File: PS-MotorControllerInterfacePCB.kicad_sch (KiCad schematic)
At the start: 10 parts, among them U2 MCP16331x-xCH

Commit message: sch
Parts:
- added D4, D8: LED, symbol Device:LED
- added D5, D7: 1N4148WT, Diode_SMD:D_SOD-523, symbol Diode:1N4148WT
- added FID1, FID2, FID3: Fiducial, symbol Mechanical:Fiducial
- added H1, H2, H3, H4: MountingHole, symbol Mechanical:MountingHole
- added J1: 53307-2471, UTSVT_Connectors:PeripheralSOM, symbol utsvt_connectors:PeripheralSOMConnector
- added J2: MotorController-in, symbol Connector_Generic:Conn_02x03_Top_Bottom
- added J3: Conn_01x06, symbol Connector_Generic:Conn_01x06
- added J4: PEAK, symbol Connector_Generic:Conn_01x02
- added J6: MotorController-out, symbol Connector_Generic:Conn_02x03_Top_Bottom
- added LVPWR1, LVPWR2, LVPWR3, LVPWR4, LVPWR5, LVPWR6: LED, LED_SMD:LED_0603_1608Metric, symbol Device:LED
- added R15, R3, R4, R5, R8: 260, symbol Device:R
- added R6, R7, R9: 4.3k, symbol Device:R
- added R_A_TACH_PD1, R_B_TACH_PD1: 10k, symbol Device:R
- added TP1, TP2, TP3, TP4, TP5, TP6: TestPoint, symbol Connector:TestPoint
- added TVS1: PTVS5V0Z1USK, Diode_SMD:Nexperia_DSN1608-2_1.6x0.8mm, symbol Diode:PTVS5V0Z1USK
- C1: value C -> 100n
- C2, C3: value C -> 22u
- D3: value 1N47xxA -> 1N47xxA 7.5V
- L1: value 56m -> 56u
- R1: value R -> 140k
- R2: value R -> 10k
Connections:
- net GND: now also J1.1 (GND), J1.10 (GNDA), J1.3 (GND), J1.5 (GND), J2.2 (Pin_2), J3.2 (Pin_2), LVPWR1.1 (K), LVPWR2.1 (K), LVPWR3.1 (K), LVPWR4.1 (K), LVPWR5.1 (K), LVPWR6.1 (K), TP1.1, TVS1.2 (A)
- net VIN renamed +24V
- net +24V: now also J1.24 (+24V_In), J3.1 (Pin_1), R7.2, TVS1.1 (K)
- net VOUT renamed 12V_BUS
- new net: LVPWR5.2 (A), R8.1
- new net: LVPWR2.2 (A), R3.1
- new net: LVPWR6.2 (A), R15.1
- new net: D4.2 (A), R9.1
- new net: D8.2 (A), R6.1
- new net: LVPWR4.2 (A), R5.1
- new net: LVPWR3.2 (A), R4.1
- new net: LVPWR1.2 (A), R7.1
- new net +12V: J2.1 (Pin_1)
- new net +3V3: J1.2 (+3.3v), R3.2, R_A_TACH_PD1.2, R_B_TACH_PD1.2
- new net CAN_H-in: J2.4 (Pin_4), J3.3 (Pin_3), J4.1 (Pin_1)
- new net CAN_H-out: J1.22 (CAN_H), J6.4 (Pin_4)
- new net CAN_L-in: J2.5 (Pin_5), J3.4 (Pin_4), J4.2 (Pin_2)
- new net CAN_L-out: J1.20 (CAN_L), J6.5 (Pin_5)
- new net FANS_A_NEG: D7.2 (A), D8.1 (K)
- new net FANS_B_NEG: D4.1 (K), D5.2 (A)
- new net FANS_POS: D5.1 (K), D7.1 (K), R6.2, R9.2
- new net FAN_A_TACHO: J1.23 (SPI1_SCK), R5.2, R_A_TACH_PD1.1
- new net FAN_B_TACHO: J1.21 (SPI1_MISO), R8.2, R_B_TACH_PD1.1
- new net PWM_FAN_A: J1.18 (SPI2_SCK), R4.2
- new net PWM_FAN_B: J1.13 (ADC1_IN10), R15.2
- no-connect marks 1 -> 30
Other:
- added sheet Fans (Fans.kicad_sch)
- added sheet Power (Power.kicad_sch)
- note added: "Fiducials"
- note added: "Indicator LEDs"
- note added: "LV PWR indicator LED"
- note added: "Mounting Holes"
- note added: "PSOM"
- note added: "PWR + CAN Connector"
- note added: "Pick TVS with VRWM > LV"
- note added: "Pin: PA11 ; TIM1_CH4"
- note added: "Pin: PA5 ; TIM2_CH1"
- note added: "Pin: PB10 ; TIM2_CH3"
- note added: "Pin: PB3 ; TIM2_CH2"
- note added: "Protection"
- note added: "Testpoints"
- note added: "put close to fan connector and mosfet for small inductive loop"
- note added: "put these near MCU input"
- moved on the sheet: C1, C2, C3, D1, D2, D3, L1, R1, R2, U2

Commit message: schematic
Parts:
- removed C1: 100n, symbol Device:C
- removed C2, C3: 22u, symbol Device:C
- removed D1: D_Schottky, symbol Device:D_Schottky
- removed D2, D5, D7: 1N4148WT, Diode_SMD:D_SOD-523, symbol Diode:1N4148WT
- removed D3: 1N47xxA 7.5V, Diode_THT:D_DO-41_SOD81_P10.16mm_Horizontal, symbol Diode:1N47xxA
- removed D4, D8: LED, symbol Device:LED
- removed FID1, FID2, FID3: Fiducial, symbol Mechanical:Fiducial
- removed H1, H2, H3, H4: MountingHole, symbol Mechanical:MountingHole
- removed L1: 56u, symbol Device:L
- removed LVPWR3, LVPWR4, LVPWR5, LVPWR6: LED, LED_SMD:LED_0603_1608Metric, symbol Device:LED
- removed R1: 140k, symbol Device:R
- removed R15, R4, R5, R8: 260, symbol Device:R
- removed R2: 10k, symbol Device:R
- removed R9: 4.3k, symbol Device:R
- removed U2: MCP16331x-xCH, Package_TO_SOT_SMD:SOT-23-6, symbol Regulator_Switching:MCP16331x-xCH
- added H1, H2, H3, H4: MountingHole_Pad, symbol Mechanical:MountingHole_Pad
- added JP1: TRM, Connector_PinHeader_2.54mm:PinHeader_1x02_P2.54mm_Vertical, symbol Jumper:Jumper_2_Open
- added LVPWR7: LED, LED_SMD:LED_0603_1608Metric, symbol Device:LED
- added R17: 120, Resistor_SMD:R_0603_1608Metric_Pad0.98x0.95mm_HandSolder, symbol Device:R
- R6: value 4.3k -> 1.9k
- TP1: value TestPoint -> TP_GND
- TP2: value TestPoint -> TP_3V3
- TP3: value TestPoint -> TP_A_TACH
- TP4: value TestPoint -> TP_B_TACH
- TP5: value TestPoint -> TP_B_PWM
- TP6: value TestPoint -> TP_A_PWM
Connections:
- net FANS_POS is gone; now on net +12V: R6.2
- net +24V: no longer J3.1 (Pin_1)
- net +3V3: now also TP2.1
- net CAN_H-out: now also J3.5 (Pin_5), R17.1
- net CAN_L-out: now also J3.6 (Pin_6), JP1.2 (B)
- net FAN_A_TACHO: now also TP3.1
- net FAN_B_TACHO: now also TP4.1
- net GND: now also H1.1, H2.1, H3.1, H4.1, LVPWR7.1 (K); no longer J1.10 (GNDA)
- net PWM_FAN_A: now also TP6.1
- net PWM_FAN_B: now also TP5.1
- net at R6.1: now also LVPWR7.2 (A)
- new net: JP1.1 (A), R17.2
- new net VIN_24V: J3.1 (Pin_1)
- no-connect marks 30 -> 23
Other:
- added sheet Buck Converter 24V-12V (BuckConverter.kicad_sch)
- added sheet Fuses (Fuses.kicad_sch)
- note added: "(12-2.5)/(.005) = 1.9k"
- note added: "(24-2.5)/(.005) = 4.3k"
- note added: "(3.3-2.5)/(.005) = 260"
- note added: "CAN Bus Termination"
- note added: "Pick TVS with VRWM > LV (24V)"
- note added: "Route PSOM Last reduce signal reflection"
- note added: "TVS"
- note added: "VCU -> moco-in -> moco-out -> interface terminate on VCU and interface"
- note added: "put PUs near MCU input"
- note removed: "BUCK CONVERTER 24V-12V"
- note removed: "Fiducials"
- note removed: "Pick TVS with VRWM > LV"
- note removed: "Protection"
- note removed: "Testpoints"
- note removed: "put close to fan connector and mosfet for small inductive loop"
- note removed: "put these near MCU input"
- moved on the sheet: J1, J2, J3, J4, J6, LVPWR1, LVPWR2, R3, R7, R_A_TACH_PD1, R_B_TACH_PD1, TVS1

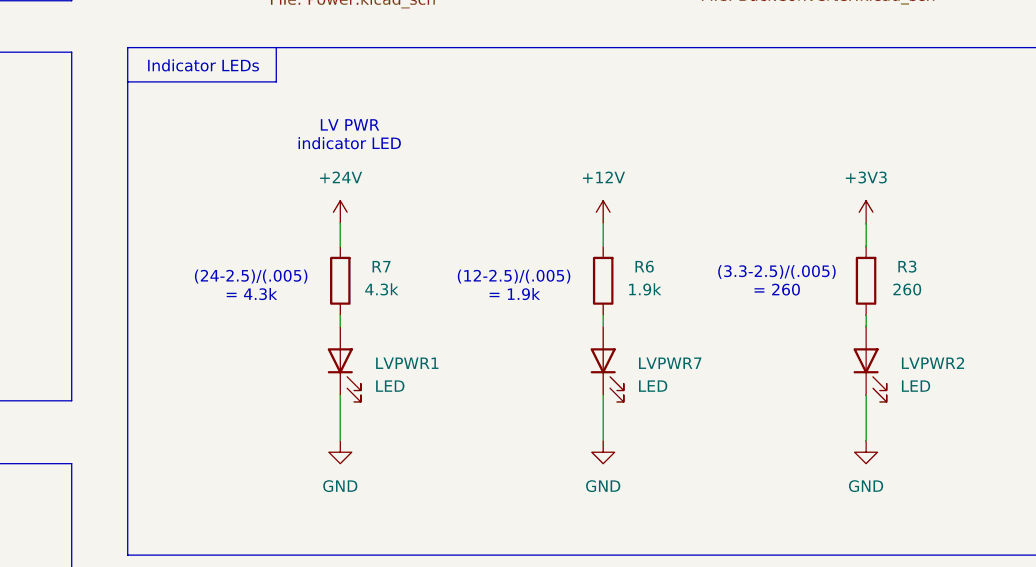
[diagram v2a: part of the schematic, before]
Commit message: added testpoints too
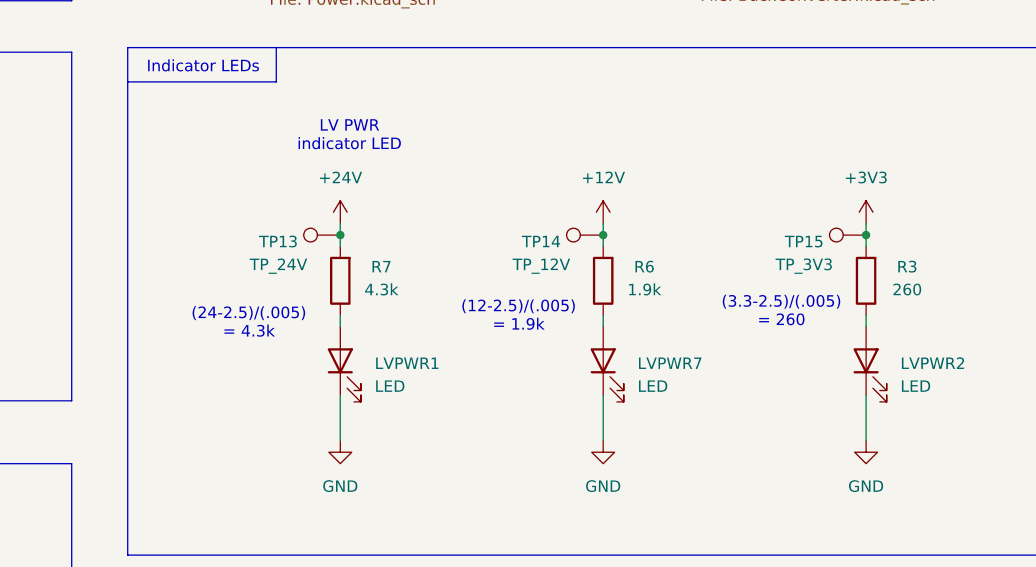
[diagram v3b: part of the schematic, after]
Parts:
- added TP13: TP_24V, symbol Connector:TestPoint
- added TP14: TP_12V, symbol Connector:TestPoint
- added TP15: TP_3V3, symbol Connector:TestPoint
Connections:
- net +12V: now also TP14.1
- net +24V: now also TP13.1
- net +3V3: now also TP15.1
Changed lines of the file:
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@@
 	(text "(24-2.5)/(.005) \n= 4.3k"
 		(exclude_from_sim no)
-		(at 190.754 130.302 0)
+		(at 190.5 134.366 0)
 		(effects
 			(font
@@
 	(text "(12-2.5)/(.005) \n= 1.9k"
 		(exclude_from_sim no)
-		(at 219.964 130.302 0)
+		(at 220.472 133.604 0)
 		(effects
 			(font
@@
 	(text "(3.3-2.5)/(.005) \n= 260"
 		(exclude_from_sim no)
-		(at 249.174 129.794 0)
+		(at 249.682 133.096 0)
 		(effects
 			(font
@@
 	)
 	(junction
+		(at 200.66 124.46)
+		(diameter 0)
+		(color 0 0 0 0)
+	)
+	(junction
 		(at 52.07 78.74)
 		(diameter 0)
@@
 	)
 	(junction
+		(at 259.08 124.46)
+		(diameter 0)
+		(color 0 0 0 0)
+	)
+	(junction
 		(at 133.35 57.15)
 		(diameter 0)
@@
 	)
 	(junction
+		(at 229.87 124.46)
+		(diameter 0)
+		(color 0 0 0 0)
+	)
+	(junction
 		(at 46.99 83.82)
 		(diameter 0)
@@
 	(wire
 		(pts
-			(xy 229.87 123.19) (xy 229.87 125.73)
+			(xy 229.87 123.19) (xy 229.87 124.46)
 		)
 		(stroke
@@
 	(wire
 		(pts
+			(xy 229.87 124.46) (xy 229.87 125.73)
+		)
+		(stroke
+			(width 0)
+			(type default)
+		)
+	)
+	(wire
+		(pts
 			(xy 187.96 81.28) (xy 191.77 81.28)
 		)
@@
 	(wire
 		(pts
-			(xy 200.66 123.19) (xy 200.66 125.73)
+			(xy 200.66 123.19) (xy 200.66 124.46)
 		)
 		(stroke
@@
 	(wire
 		(pts
+			(xy 259.08 124.46) (xy 259.08 125.73)
+		)
+		(stroke
+			(width 0)
+			(type default)
+		)
+	)
+	(wire
+		(pts
 			(xy 133.35 53.34) (xy 133.35 57.15)
 		)
@@
 	(wire
 		(pts
-			(xy 259.08 123.19) (xy 259.08 125.73)
+			(xy 200.66 124.46) (xy 200.66 125.73)
+		)
+		(stroke
+			(width 0)
+			(type default)
+		)
+	)
+	(wire
+		(pts
+			(xy 259.08 123.19) (xy 259.08 124.46)
 		)
 		(stroke
@@
 	)
 	(symbol
+		(lib_id "Connector:TestPoint")
+		(at 200.66 124.46 90)
+		(unit 1)
+		(exclude_from_sim no)
+		(in_bom yes)
+		(on_board yes)
+		(dnp no)
+		(property "Reference" "TP13"
+			(at 193.802 125.222 90)
+			(effects
+				(font
+					(size 1.27 1.27)
+				)
+			)
+		)
+		(property "Value" "TP_24V"
+			(at 193.802 127.762 90)
+			(effects
+				(font
+					(size 1.27 1.27)
+				)
+			)
+		)
+		(property "Footprint" ""
+			(at 200.66 119.38 0)
+			(effects
+				(font
+					(size 1.27 1.27)
+				)
+				(hide yes)
+			)
+		)
+		(property "Datasheet" "~"
+			(at 200.66 119.38 0)
+			(effects
+				(font
+					(size 1.27 1.27)
+				)
+				(hide yes)
+			)
+		)
+		(property "Description" "test point"
+			(at 200.66 124.46 0)
+			(effects
+				(font
+					(size 1.27 1.27)
+				)
+				(hide yes)
+			)
+		)
+		(pin "1"
+		)
+		(instances
+			(project "PS-MotorControllerInterfacePCB"
+				(path "/a2e13c19-ff3a-4e43-a7f5-200fd5b2b978"
+					(reference "TP13")
+					(unit 1)
+				)
+			)
+		)
+	)
+	(symbol
 		(lib_id "Connector_Generic:Conn_02x03_Top_Bottom")
 		(at 48.26 181.61 0)
@@
 	)
 	(symbol
+		(lib_id "Connector:TestPoint")
+		(at 259.08 124.46 90)
+		(unit 1)
+		(exclude_from_sim no)
+		(in_bom yes)
+		(on_board yes)
+		(dnp no)
+		(property "Reference" "TP15"
+			(at 252.222 125.222 90)
+			(effects
+				(font
+					(size 1.27 1.27)
+				)
+			)
+		)
+		(property "Value" "TP_3V3"
+			(at 252.222 127.762 90)
+			(effects
+				(font
+					(size 1.27 1.27)
+				)
+			)
+		)
+		(property "Footprint" ""
+			(at 259.08 119.38 0)
+			(effects
+				(font
+					(size 1.27 1.27)
+				)
+				(hide yes)
+			)
+		)
+		(property "Datasheet" "~"
+			(at 259.08 119.38 0)
+			(effects
+				(font
+					(size 1.27 1.27)
+				)
+				(hide yes)
+			)
+		)
+		(property "Description" "test point"
+			(at 259.08 124.46 0)
+			(effects
+				(font
+					(size 1.27 1.27)
+				)
+				(hide yes)
+			)
+		)
+		(pin "1"
+		)
+		(instances
+			(project "PS-MotorControllerInterfacePCB"
+				(path "/a2e13c19-ff3a-4e43-a7f5-200fd5b2b978"
+					(reference "TP15")
+					(unit 1)
+				)
+			)
+		)
+	)
+	(symbol
 		(lib_id "Device:R")
 		(at 229.87 129.54 180)
@@
 					(unit 1)
 				)
+			)
+		)
+	)
+	(symbol
+		(lib_id "Connector:TestPoint")
+		(at 229.87 124.46 90)
+		(unit 1)
+		(exclude_from_sim no)
+		(in_bom yes)
+		(on_board yes)
+		(dnp no)
+		(property "Reference" "TP14"
+			(at 223.012 125.222 90)
+			(effects
+				(font
+					(size 1.27 1.27)
+				)
+			)
+		)
+		(property "Value" "TP_12V"
+			(at 223.012 127.762 90)
+			(effects
+				(font
+					(size 1.27 1.27)
+				)
+			)
+		)
+		(property "Footprint" ""
+			(at 229.87 119.38 0)
+			(effects
+				(font
+					(size 1.27 1.27)
+				)
+				(hide yes)
+			)
+		)
+		(property "Datasheet" "~"
+			(at 229.87 119.38 0)
+			(effects
+				(font
+					(size 1.27 1.27)
+				)
+				(hide yes)
+			)
+		)
+		(property "Description" "test point"
+			(at 229.87 124.46 0)
+			(effects
+				(font
+					(size 1.27 1.27)
+				)
+				(hide yes)
+			)
+		)
+		(pin "1"
+		)
+		(instances
+			(project "PS-MotorControllerInterfacePCB"
+				(path "/a2e13c19-ff3a-4e43-a7f5-200fd5b2b978"
+					(reference "TP14")
+					(unit 1)
+				)

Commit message: changes + ioc
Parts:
- added LVPWR4, LVPWR5, LVPWR8, LVPWR9: LED, LED_SMD:LED_0603_1608Metric, symbol Device:LED
- added R11: 100k, Resistor_SMD:R_0603_1608Metric, symbol Device:R_US
- added R12: 9。5k, Resistor_SMD:R_0603_1608Metric, symbol Device:R_US
- added R18: 200k, Resistor_SMD:R_0603_1608Metric, symbol Device:R_US
- added R21, R22, R5, R8: 5k, symbol Device:R
- added R25: 9k, Resistor_SMD:R_0603_1608Metric, symbol Device:R_US
- added TP9: TP_3V3, symbol Connector:TestPoint
- added Z1, Z2: SMAF4751A-TP, UTSVT_Passives:SODFL5026X125N, symbol UTSVT_Power:SMAF4749A-TP
- added Z3, Z4: SMAF4744A, UTSVT_Passives:SODFL5026X125N, symbol UTSVT_Power:SMAF4749A-TP
- R3: value 260 -> 5k
- R6: value 1.9k -> 5k
- R7: value 4.3k -> 5k
- TP2: value TP_3V3 -> TP_24V
- TP5: value TP_B_PWM -> TP_12V
- TP6: value TP_A_PWM -> TP_3V3
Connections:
- net +3V3: no longer TP2.1
- net 12V_BUS: now also R11.1, Z4.1 (K)
- net CAN_H-out: no longer J3.5 (Pin_5), J6.4 (Pin_4)
- net CAN_L-out: no longer J3.6 (Pin_6), J6.5 (Pin_5)
- net GND: now also LVPWR4.1 (K), LVPWR5.1 (K), LVPWR8.1 (K), LVPWR9.1 (K), R12.2, R25.2, Z1.2 (A), Z2.2 (A), Z3.2 (A), Z4.2 (A); no longer H1.1, H2.1, H3.1, H4.1
- net PWM_FAN_A: no longer TP6.1
- net PWM_FAN_B: no longer TP5.1
- net VIN_24V: now also R18.1, Z1.1 (K)
- net LED2: now reaches J1.11 (ADC1_IN9)
- net D_C: now reaches J1.12 (SPI2_NSS)
- net D_C: now also TP6.1, R21.2
- net M_FAULT: now reaches J1.14 (SPI2_MISO)
- net M_FAULT: now also R22.2, TP9.1
- net LED3: now reaches J1.15 (ADC1_IN11)
- net LED: now reaches J1.16 (SPI2_MOSI)
- net LED5: now reaches J1.17 (SPI1_MOSI)
- net LED4: now reaches J1.19 (SPI1_NSS)
- net S_OC: now reaches J1.4 (I2C1_SDA)
- net S_OC: now also TP5.1, R8.2
- net MESSAGE: now reaches J1.6 (I2C1_SCL)
- net MESSAGE: now also TP2.1, R5.2
- net LED1: now reaches J1.9 (ADC1_IN7)
- net CAN_H-in renamed CAN_H
- net CAN_H: now also J3.5 (Pin_5), J6.4 (Pin_4)
- net CAN_L-in renamed CAN_L
- net CAN_L: now also J3.6 (Pin_6), J6.5 (Pin_5)
- new net: LVPWR4.2 (A), R5.1
- new net: LVPWR9.2 (A), R22.1
- new net: LVPWR8.2 (A), R21.1
- new net: LVPWR5.2 (A), R8.1
- new net Power12V/OV: R11.2, R12.1
- new net Power24V/OV: R18.2, R25.1
- new net RPP_EN12: Z3.1 (K)
- new net RPP_EN24: Z2.1 (K)
- no-connect marks 23 -> 17
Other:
- sheet Fuses renamed Fuse
- removed sheet Power
- added sheet Power12V (Power.kicad_sch)
- added sheet Power24V (Power.kicad_sch)
- added sheet StatusLEDs (StatusLEDs.kicad_sch)
- note added: "PA12"
- note added: "PA2"
- note added: "PA4"
- note added: "PA6"
- note added: "PB0"
- note added: "PB15"
- note added: "Pin: PB12"
- note added: "Pin: PB14"
- note added: "Pin: PB6"
- note added: "Pin: PB7"
- note removed: "(12-2.5)/(.005) = 1.9k"
- note removed: "(24-2.5)/(.005) = 4.3k"
- note removed: "(3.3-2.5)/(.005) = 260"
- moved on the sheet: H1, H2, H3, H4, JP1, LVPWR1, LVPWR2, LVPWR7, R17, R3, R6, R7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

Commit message: small fix
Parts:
- TP2: value TP_24V -> TP_M
- TP5: value TP_12V -> TP_OC
- TP6: value TP_3V3 -> TP_D_C
- TP9: value TP_3V3 -> TP_F
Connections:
- net CAN_H-out is gone; now on net CAN_H: J1.22 (CAN_H), R17.1
- net CAN_L-out is gone; now on net CAN_L: J1.20 (CAN_L), JP1.2 (B)
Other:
- note added: "PB14"
- note added: "PB6"
- note added: "PB7"
- note removed: "Pin: PB14"
- note removed: "Pin: PB6"
- note removed: "Pin: PB7"
- moved on the sheet: J1, J2, J3, J4, J6, JP1, LVPWR1, LVPWR2, LVPWR4, LVPWR5, LVPWR7, LVPWR8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

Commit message: layout
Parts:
- removed TP13: TP_24V, symbol Connector:TestPoint
- removed TP14: TP_12V, symbol Connector:TestPoint
- added J5: Power MPPT, UTSVT_Connectors:Molex_Nano-Fit_105309-xx02_1x02_P2.50mm_Vertical, symbol Connector_Generic:Conn_01x02
- H1, H2, H3, H4: footprint (none) -> MountingHole:MountingHole_3.2mm_M3
- J2, J6: footprint (none) -> UTSVT_Connectors:Molex_Microfit3.0_02x03_6-Pin-Vertical-PCB-Receptacle_447690601
- J3: footprint (none) -> Connector_Molex:Molex_Nano-Fit_105310-xx06_2x03_P2.50mm_Vertical
- J4: footprint (none) -> Connector_Molex:Molex_Nano-Fit_105309-xx02_1x02_P2.50mm_Vertical
- R11: footprint Resistor_SMD:R_0603_1608Metric -> Resistor_SMD:R_0603_1608Metric_Pad0.98x0.95mm_HandSolder; Manufacturer_Part_Number (none) -> CRCW0603100KFKEE
- R12, R25: footprint Resistor_SMD:R_0603_1608Metric -> Resistor_SMD:R_0603_1608Metric_Pad0.98x0.95mm_HandSolder
- R17: Manufacturer_Part_Number (none) -> CRCW0603120RFKEC
- R18: footprint Resistor_SMD:R_0603_1608Metric -> Resistor_SMD:R_0603_1608Metric_Pad0.98x0.95mm_HandSolder; Manufacturer_Part_Number (none) -> MCT06030C2003FP500
- R21, R22, R3, R5, R6, R7, R8: value 5k -> 4.3k; footprint (none) -> Resistor_SMD:R_0603_1608Metric_Pad0.98x0.95mm_HandSolder; Manufacturer_Part_Number (none) -> CRCW06034K30FKEA
- R_A_TACH_PD1, R_B_TACH_PD1: footprint (none) -> Resistor_SMD:R_0603_1608Metric_Pad0.98x0.95mm_HandSolder; Manufacturer_Part_Number (none) -> CRCW060310K0FKEI
- TP1, TP15, TP2, TP3, TP4, TP5, TP6, TP9: footprint (none) -> TestPoint:TestPoint_Pad_1.0x1.0mm
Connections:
- net +24V: now also J5.1 (Pin_1); no longer TVS1.1 (K)
- net GND: now also J5.2 (Pin_2)
- net VIN_24V: now also TVS1.1 (K)
- net CAN_H renamed CAN_P
- net CAN_L renamed CAN_N
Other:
- moved on the sheet: H1, H2, H3, H4, J2, J3, J4, J6, JP1, LVPWR1, LVPWR2, LVPWR4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

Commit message: added more
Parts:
- J3: footprint Connector_Molex:Molex_Nano-Fit_105310-xx06_2x03_P2.50mm_Vertical -> Connector_Molex:Molex_Nano-Fit_105309-xx06_1x06_P2.50mm_Vertical
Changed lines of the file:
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@@
 			)
 		)
-		(property "Footprint" "Connector_Molex:Molex_Nano-Fit_105310-xx06_2x03_P2.50mm_Vertical"
+		(property "Footprint" "Connector_Molex:Molex_Nano-Fit_105309-xx06_1x06_P2.50mm_Vertical"
 			(at 59.69 128.27 0)
 			(effects

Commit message: new review this
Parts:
- renumbered TP15 to 3V3, TP6 to D_C, TP9 to Fault, TP2 to Message, TP5 to OVC
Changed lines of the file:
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@@
 		(on_board yes)
 		(dnp no)
-		(property "Reference" "TP5"
+		(property "Reference" "OVC"
 			(at 237.744 121.158 90)
 			(effects
@@
 			(project "PS-MotorControllerInterfacePCB"
 				(path "/a2e13c19-ff3a-4e43-a7f5-200fd5b2b978"
-					(reference "TP5")
+					(reference "OVC")
 					(unit 1)
 				)
@@
 		(on_board yes)
 		(dnp no)
-		(property "Reference" "TP6"
+		(property "Reference" "D_C"
 			(at 246.888 120.904 90)
 			(effects
@@
 			(project "PS-MotorControllerInterfacePCB"
 				(path "/a2e13c19-ff3a-4e43-a7f5-200fd5b2b978"
-					(reference "TP6")
+					(reference "D_C")
 					(unit 1)
 				)
@@
 		(on_board yes)
 		(dnp no)
-		(property "Reference" "TP15"
+		(property "Reference" "3V3"
 			(at 215.138 120.904 90)
 			(effects
@@
 			(project "PS-MotorControllerInterfacePCB"
 				(path "/a2e13c19-ff3a-4e43-a7f5-200fd5b2b978"
-					(reference "TP15")
+					(reference "3V3")
 					(unit 1)
 				)
@@
 		(on_board yes)
 		(dnp no)
-		(property "Reference" "TP9"
+		(property "Reference" "Fault"
 			(at 257.048 120.904 90)
 			(effects
@@
 			(project "PS-MotorControllerInterfacePCB"
 				(path "/a2e13c19-ff3a-4e43-a7f5-200fd5b2b978"
-					(reference "TP9")
+					(reference "Fault")
 					(unit 1)
 				)
@@
 		(on_board yes)
 		(dnp no)
-		(property "Reference" "TP2"
+		(property "Reference" "Message"
 			(at 226.822 121.158 90)
 			(effects
@@
 			(project "PS-MotorControllerInterfacePCB"
 				(path "/a2e13c19-ff3a-4e43-a7f5-200fd5b2b978"
-					(reference "TP2")
+					(reference "Message")
 					(unit 1)
 				)
